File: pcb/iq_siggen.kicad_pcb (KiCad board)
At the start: 4 copper layers, 100 x 100 mm, 267 parts, among them J1 J3 - BANK0, J10 Barrel_Jack_MountingPin, J11 Conn_Coaxial, J12 Conn_01x01_Male, J13 Conn_01x01_Male, J14 Conn_01x01_Male, J15 Conn_01x01_Male, J16 Conn_01x01_Male, J17 Conn_01x01_Male, J18 Conn_Coaxial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

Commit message: routing the dac wires
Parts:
- removed R1, R9: 0, Resistor_SMD:R_0603_1608Metric
- TP51, TP52, TP53, TP56, TP57, TP58: footprint TestPoint:TestPoint_Pad_D1.5mm -> TestPoint:TestPoint_Pad_D1.0mm
- moved R91 196.8 mm to (57.2, 138.8)
- moved R88 194.6 mm to (56.8, 141.2)
- moved R7 192.0 mm to (69.9, 88.7), turned to 180 degrees
- moved FB5 171.7 mm to (28.5, 85.9), turned to 180 degrees
- moved R8 164.1 mm to (72.2, 88.0), turned to 90 degrees
- moved C58 145.7 mm to (77.2, 81.2), turned to 180 degrees
- moved C55 144.2 mm to (77.2, 82.8), turned to 180 degrees
- moved C53 134.9 mm to (83.7, 92.2), turned to 90 degrees
- moved C62 134.3 mm to (68.5, 92.5), turned to 90 degrees
- moved C61 133.7 mm to (85.2, 92.2), turned to 90 degrees
- moved C57 132.3 mm to (70.1, 92.5), turned to 90 degrees
- moved R37 132.3 mm to (105.5, 70.9), turned to 270 degrees
- moved C49 131.6 mm to (71.6, 92.5), turned to 90 degrees
- moved C63 129.8 mm to (77.2, 79.7), turned to 180 degrees
- moved C54 128.5 mm to (73.1, 92.5), turned to 90 degrees
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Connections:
- J1 pad 10: Net-(J1-Pad10) -> /DAC_CLK_P
- J1 pad 9: Net-(J1-Pad9) -> /DAC_CLK_N
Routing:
- net /DAC_CLK_N: track 0.00 -> 92.0 mm
- net /DAC_CLK_P: track 0.00 -> 91.2 mm
- net /A9: track 4.30 -> 31.7 mm
- net Net-(J2-Pad9): track 0.00 -> 26.7 mm, vias 0 -> 2
- net /B0: track 4.05 -> 29.7 mm
- net /A8: track 4.25 -> 29.5 mm
- net GNDA: track 127.5 -> 152.7 mm, vias 73 -> 82
- net /B1: track 4.00 -> 26.9 mm
- net /A7: track 4.19 -> 26.4 mm
- net /B2: track 3.94 -> 24.7 mm
- net /B5: track 3.77 -> 24.3 mm
- net /A6: track 4.14 -> 23.8 mm
- net /B3: track 3.89 -> 22.8 mm
- net /B6: track 3.72 -> 22.1 mm
- net /A5: track 4.08 -> 22.0 mm
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
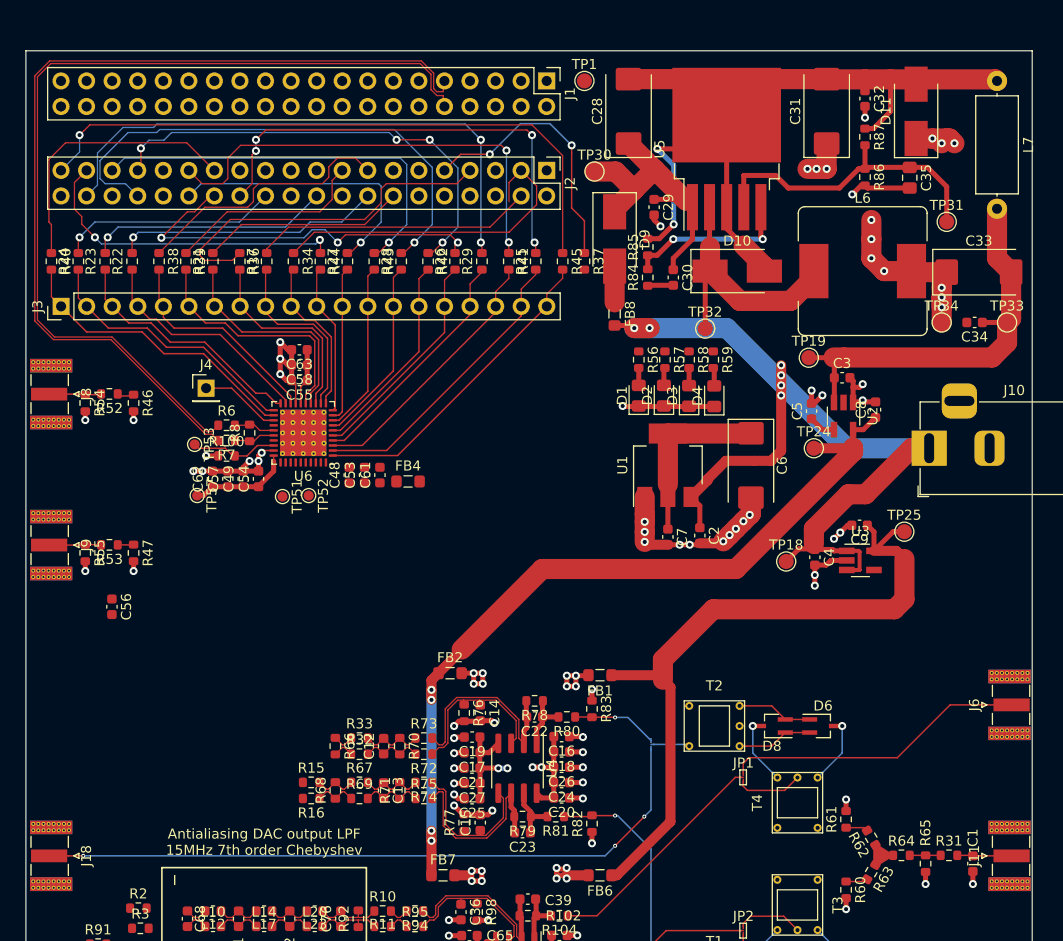
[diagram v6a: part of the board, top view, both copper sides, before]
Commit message: laying out split gnd pours
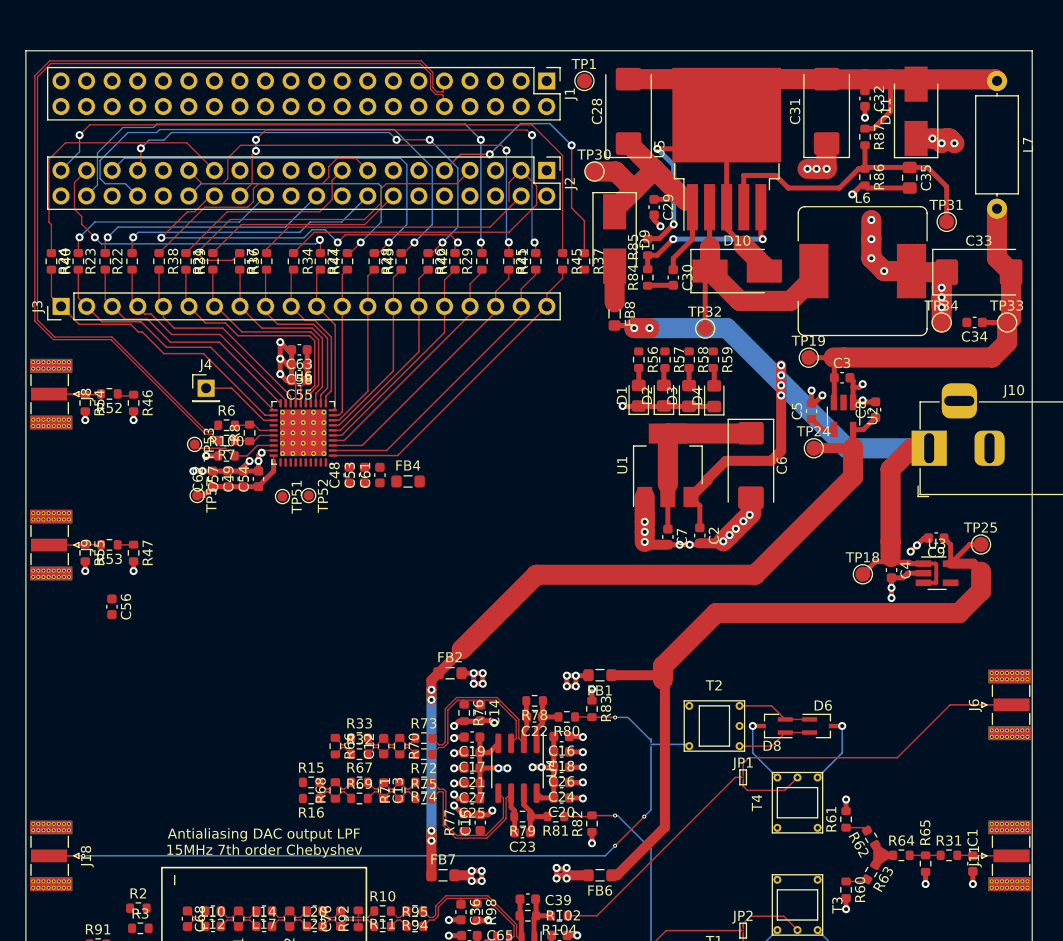
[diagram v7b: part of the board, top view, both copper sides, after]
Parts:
- U6: footprint Package_DFN_QFN:QFN-40-1EP_6x6mm_P0.5mm_EP4.6x4.6mm_ThermalVias -> iq_siggen:qfn_max5853
- moved U3 7.73 mm to (140.5, 101.9)
- moved C4 7.73 mm to (136.0, 101.6)
- moved TP25 7.73 mm to (144.9, 99.1)
- moved TP18 7.73 mm to (133.2, 102.0)
- moved C9 7.73 mm to (140.5, 98.4)
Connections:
- C29 pad 2: GNDA -> GNDPWR
- C31 pad 1: GNDA -> GNDPWR
- C32 pad 2: GNDA -> GNDPWR
- C33 pad 1: GNDA -> GNDPWR
- C34 pad 2: GNDA -> GNDPWR
- C35 pad 2: GNDA -> GNDPWR
- C49 pad 2: GNDA -> GNDS
- C54 pad 2: GNDA -> GNDS
- C55 pad 2: GNDA -> GNDD
- C57 pad 2: GNDA -> GNDS
- C58 pad 2: GNDA -> GNDD
- C62 pad 2: GNDA -> GNDS
- C63 pad 2: GNDA -> GNDD
- D1 pad 1: GNDA -> GNDD
- D11 pad 1: GNDA -> GNDPWR
- D2 pad 1: GNDA -> GNDD
- D3 pad 1: GNDA -> GNDD
- D4 pad 1: GNDA -> GNDD
- J1 pad 11: GNDA -> GNDD
- J1 pad 12: GNDA -> GNDD
- J1 pad 21: GNDA -> GNDD
- J1 pad 22: GNDA -> GNDD
- J1 pad 31: GNDA -> GNDD
- J1 pad 32: GNDA -> GNDD
- J1 pad 39: GNDA -> GNDD
- J10 pad 2: GNDA -> GNDPWR
- J2 pad 11: GNDA -> GNDD
- J2 pad 12: GNDA -> GNDD
- J2 pad 21: GNDA -> GNDD
- J2 pad 22: GNDA -> GNDD
- J2 pad 31: GNDA -> GNDD
- J2 pad 32: GNDA -> GNDD
- J8 pad 2: GNDA -> GNDD
- J9 pad 2: GNDA -> GNDD
- L6 pad 2: GNDA -> GNDPWR
- R100 pad 1: GNDA -> GNDS
- R46 pad 2: GNDA -> GNDD
- R47 pad 2: GNDA -> GNDD
- R48 pad 1: GNDA -> GNDD
- R49 pad 1: GNDA -> GNDD
- R50 pad 1: GNDA -> GNDD
- R51 pad 1: GNDA -> GNDD
- R54 pad 2: GNDA -> GNDD
- R55 pad 2: GNDA -> GNDD
- R86 pad 2: GNDA -> GNDPWR
- TP20 pad 1: GNDA -> GNDD
- TP21 pad 1: GNDA -> GNDS
- TP22 pad 1: GNDA -> GNDPWR
- TP34 pad 1: GNDA -> GNDPWR
- U6 pad 17: GNDA -> GNDD
- U6 pad 24: GNDA -> GNDS
- U6 pad 29: GNDA -> GNDS
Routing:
- net GNDA: track 152.7 -> 78.8 mm, vias 82 -> 52
- net GNDPWR: track 0.00 -> 35.9 mm, vias 0 -> 16
- net GNDD: track 0.00 -> 25.8 mm, vias 0 -> 8
- net GNDS: track 0.00 -> 12.2 mm, vias 0 -> 6
- net +2V5: track 70.2 -> 75.5 mm
- net +5V: track 88.0 -> 85.1 mm
- net -2V5: track 81.6 -> 83.0 mm
- added copper zone on In1.Cu, net GNDD
- added copper zone on In1.Cu, net GNDS

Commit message: routing contiued, add swtiches, remove test points, all parts now positioned on board
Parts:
- removed R20, R35: 22, Resistor_SMD:R_0603_1608Metric
- removed R50, R51: 10k, Resistor_SMD:R_0603_1608Metric
- removed TP2, TP20, TP21, TP3, TP5, TP6, TP7, TP8, TP9: TestPoint, TestPoint:TestPoint_Pad_D1.5mm
- added SW1: SW_Push, Button_Switch_THT:SW_PUSH_6mm_H5mm, F.Cu at (108.7, 98.5)
- added SW2: SW_Push, Button_Switch_THT:SW_PUSH_6mm_H5mm, F.Cu at (108.7, 109.1)
- added TP4: TestPoint, TestPoint:TestPoint_Pad_D1.5mm, F.Cu at (64.7, 91.9)
- J10: value Barrel_Jack_MountingPin -> Barrel_Jack
- moved R13 195.7 mm to (78.3, 119.9)
- moved R14 172.5 mm to (78.3, 118.3), turned to 180 degrees
- moved TP10 165.5 mm to (102.8, 67.7)
- moved R18 155.1 mm to (99.8, 96.2), turned to 90 degrees
- moved R90 153.3 mm to (73.9, 100.9), turned to 270 degrees
- moved R101 150.7 mm to (76.4, 94.0), turned to 90 degrees
- moved FB3 139.1 mm to (95.8, 85.1), turned to 270 degrees
- moved TP23 134.5 mm to (122.1, 84.5)
- moved R48 133.4 mm to (98.3, 96.2), turned to 270 degrees
- moved TP17 132.0 mm to (134.8, 89.1)
- moved TP58 130.1 mm to (93.9, 85.4)
- moved R49 127.6 mm to (112.7, 106.3), turned to 270 degrees
- moved TP22 120.4 mm to (148.0, 97.1)
- moved C38 119.5 mm to (74.9, 94.0), turned to 270 degrees
- moved R19 118.0 mm to (111.2, 106.3), turned to 90 degrees
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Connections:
- C29 pad 2: GNDPWR -> GNDA
- C31 pad 1: GNDPWR -> GNDA
- C32 pad 2: GNDPWR -> GNDA
- C33 pad 1: GNDPWR -> GNDA
- C34 pad 2: GNDPWR -> GNDA
- C35 pad 2: GNDPWR -> GNDA
- D1 pad 1: GNDD -> GNDA
- D11 pad 1: GNDPWR -> GNDA
- D2 pad 1: GNDD -> GNDA
- D3 pad 1: GNDD -> GNDA
- D4 pad 1: GNDD -> GNDA
- J1 pad 11: GNDD -> GNDS
- J1 pad 12: GNDD -> GNDS
- J1 pad 21: GNDD -> GNDA
- J1 pad 22: GNDD -> GNDA
- J1 pad 31: GNDD -> GNDA
- J1 pad 32: GNDD -> GNDA
- J1 pad 39: GNDD -> GNDA
- J1 pad 5: (no net) -> Net-(J1-Pad5)
- J1 pad 6: (no net) -> Net-(J1-Pad6)
- J10 pad 2: GNDPWR -> GNDA
- J2 pad 27: Net-(J2-Pad27) -> (no net)
- J2 pad 3: Net-(J2-Pad3) -> (no net)
- J2 pad 4: Net-(J2-Pad4) -> (no net)
- J2 pad 9: Net-(J2-Pad9) -> (no net)
- L6 pad 2: GNDPWR -> GNDA
- R17 pad 2: Net-(J2-Pad4) -> Net-(J2-Pad28)
- R18 pad 2: Net-(J2-Pad6) -> Net-(J1-Pad5)
- R19 pad 2: Net-(J2-Pad8) -> Net-(J1-Pad6)
- R21 pad 2: Net-(J2-Pad14) -> Net-(J2-Pad30)
- R22 pad 2: Net-(J2-Pad16) -> Net-(J2-Pad35)
- R23 pad 2: Net-(J2-Pad20) -> Net-(J2-Pad38)
- R24 pad 2: Net-(J2-Pad24) -> Net-(J2-Pad37)
- R25 pad 2: Net-(J2-Pad26) -> Net-(J2-Pad7)
- R26 pad 2: Net-(J2-Pad28) -> Net-(J2-Pad14)
- R27 pad 2: Net-(J2-Pad30) -> Net-(J2-Pad20)
- R28 pad 2: Net-(J2-Pad34) -> Net-(J2-Pad16)
- R29 pad 2: Net-(J2-Pad38) -> Net-(J2-Pad10)
- R34 pad 1: Net-(J2-Pad3) -> Net-(J2-Pad26)
- R36 pad 1: Net-(J2-Pad7) -> Net-(J2-Pad29)
- R37 pad 1: Net-(J2-Pad9) -> Net-(J2-Pad5)
- R38 pad 1: Net-(J2-Pad15) -> Net-(J2-Pad34)
- R39 pad 1: Net-(J2-Pad17) -> Net-(J2-Pad33)
- R40 pad 1: Net-(J2-Pad27) -> Net-(J2-Pad39)
- R41 pad 1: Net-(J2-Pad29) -> Net-(J2-Pad8)
- R42 pad 1: Net-(J2-Pad33) -> Net-(J2-Pad15)
- R43 pad 1: Net-(J2-Pad35) -> Net-(J2-Pad17)
- R44 pad 1: Net-(J2-Pad37) -> Net-(J2-Pad24)
- R45 pad 1: Net-(J2-Pad39) -> Net-(J2-Pad6)
- R48 pad 1: GNDD -> GNDA
- R49 pad 1: GNDD -> GNDA
- R86 pad 2: GNDPWR -> GNDA
- R88 pad 1: /IQ DAC and AA filter/A_IOUT_P -> /IQ DAC and AA filter/A_IOUT_N
- R89 pad 1: /IQ DAC and AA filter/A_IOUT_N -> /IQ DAC and AA filter/A_IOUT_P
- TP22 pad 1: GNDPWR -> GNDA
- TP34 pad 1: GNDPWR -> GNDA
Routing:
- net /I_CLK_P: track 0.00 -> 116.7 mm, vias 0 -> 1
- net /I_CLK_N: track 0.00 -> 116.4 mm, vias 0 -> 1
- net /Q_CLK_N: track 0.00 -> 110.2 mm, vias 0 -> 1
- net /Q_CLK_P: track 0.00 -> 109.8 mm, vias 0 -> 1
- net GNDA: track 78.8 -> 153.5 mm, vias 52 -> 89
- net /IQ DAC and AA filter/B_IOUT_N: track 0.00 -> 67.1 mm, vias 0 -> 2
- net /IQ DAC and AA filter/B_IOUT_P: track 0.00 -> 66.7 mm, vias 0 -> 2
- net /LED3: track 0.00 -> 66.4 mm, vias 0 -> 1
- net /LED2: track 0.00 -> 61.4 mm, vias 0 -> 1
- net +3V3: track 17.8 -> 76.5 mm, vias 0 -> 9
- net Net-(J1-Pad6): track 0.00 -> 58.4 mm, vias 0 -> 2
- net /IQ DAC and AA filter/A_IOUT_N: track 0.00 -> 57.9 mm, vias 0 -> 2
- net /IQ DAC and AA filter/A_IOUT_P: track 0.00 -> 57.5 mm, vias 0 -> 2
- net /LED1: track 0.00 -> 56.4 mm, vias 0 -> 1
- net Net-(J2-Pad39): track 63.9 -> 9.03 mm, vias 1 -> 0
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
